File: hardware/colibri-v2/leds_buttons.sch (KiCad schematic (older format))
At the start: 39 parts

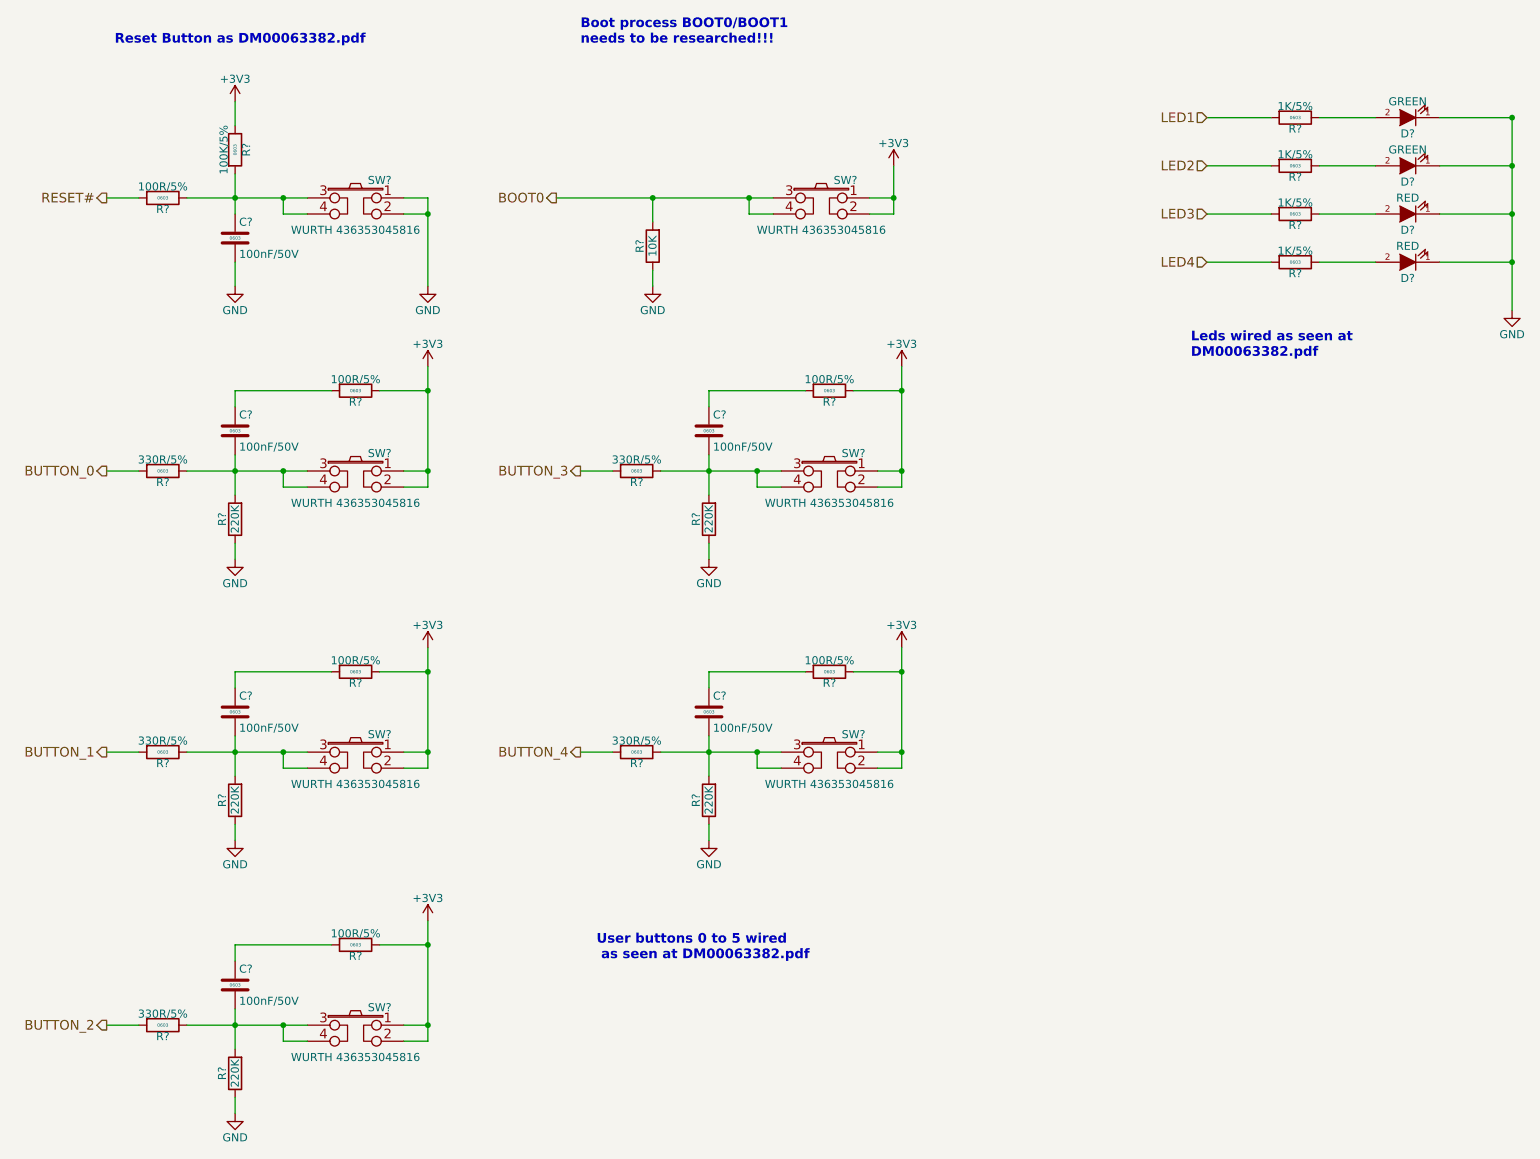
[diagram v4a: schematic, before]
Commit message: Worn on USB OTG connection for the cortex MCU
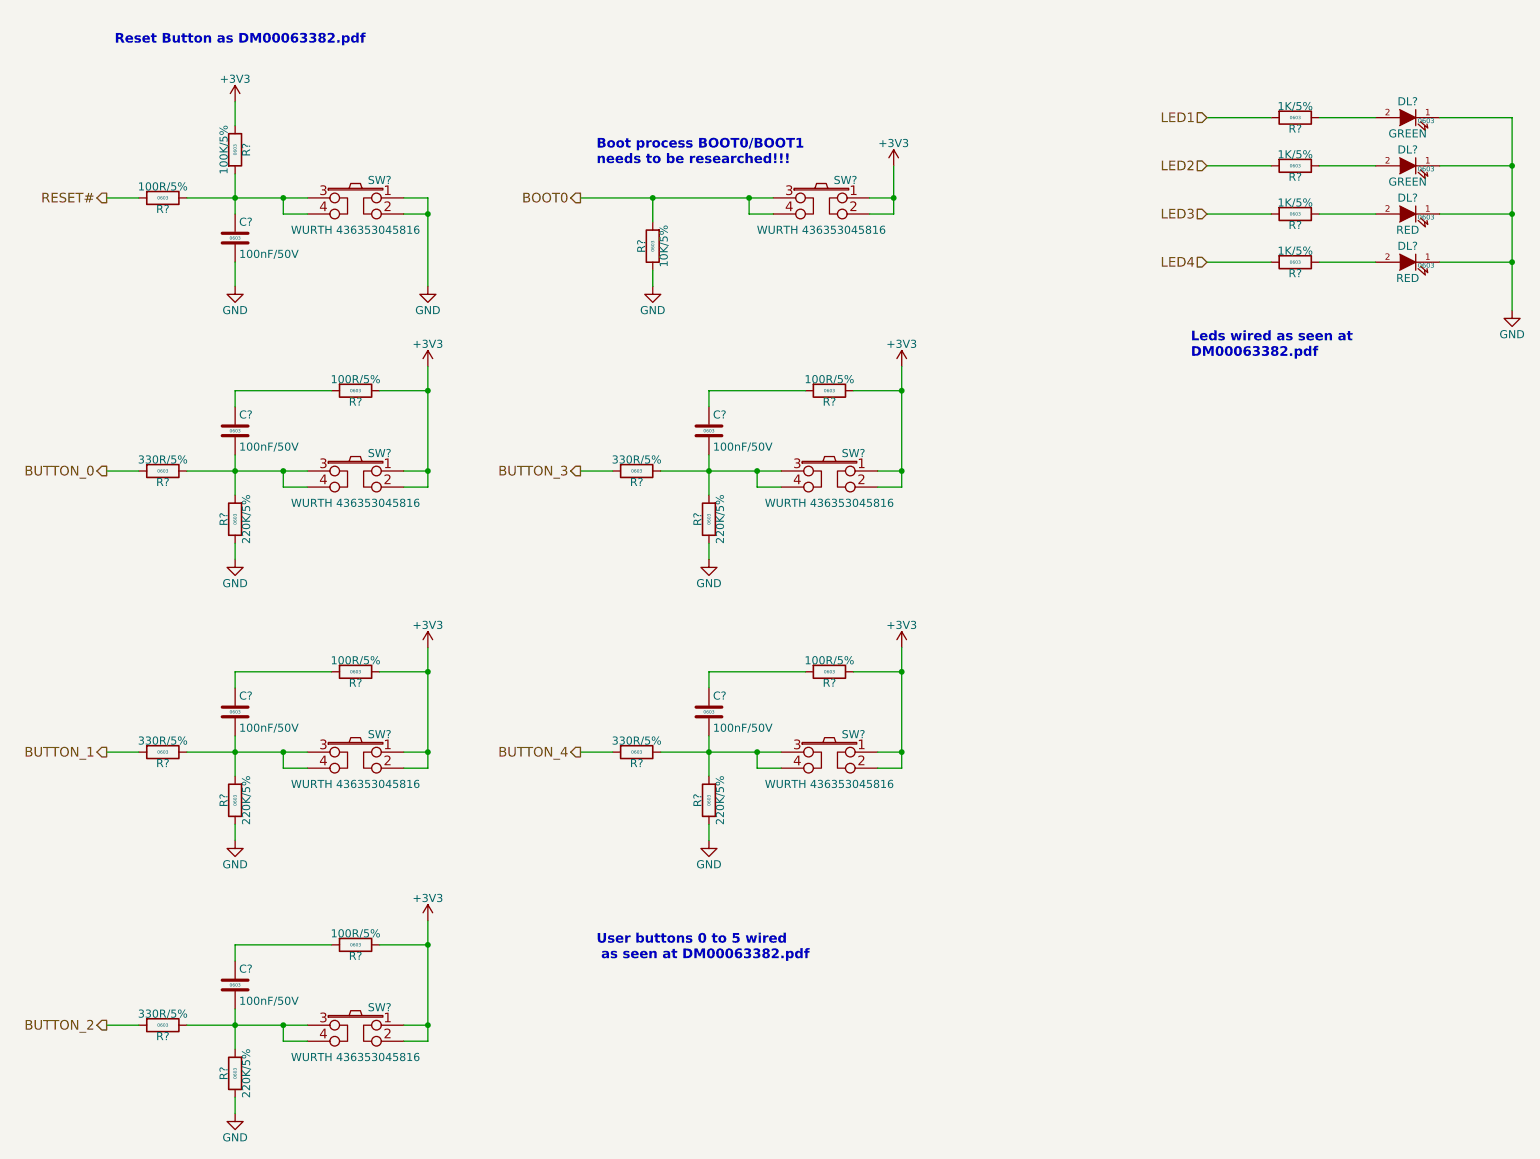
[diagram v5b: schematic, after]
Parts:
- removed D? (x2): GREEN, symbol LED
- removed D? (x2): RED, symbol LED
- removed R?: 10K, Resistors_SMD:R_0603, symbol R
- removed R? (x5): 220K, Resistors_SMD:R_0603, symbol R
- added DL? (x2): GREEN, LEDs:LED-0603, symbol LED_SMT
- added DL? (x2): RED, LEDs:LED-0603, symbol LED_SMT
- added R? (x5): 220K/5%, Resistors_SMD:R_0603, symbol R_SMT
- added R?: 10K/5%, Resistors_SMD:R_0603, symbol R_SMT
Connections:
- net BOOT0: now also R?.2
- net GND: now also DL?.1 (K), DL?.1 (K), DL?.1 (K), DL?.1 (K), R?.1, R?.1, R?.1, R?.1, R?.1, R?.1
- net at R?.1: now also DL?.2 (A) (x4)
- net at C?.2, R?.1, SW?.3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: now also R?.2 (x5)
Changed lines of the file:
@@
 Text HLabel 1350 1700 0    60   Output ~ 0
 RESET#
-$Comp
-L LED D?
-U 1 1 55862ED2
-P 9450 1200
-F 0 "D?" H 9450 1300 50  0000 C CNN
-F 1 "GREEN" H 9450 1100 50  0000 C CNN
-F 2 "" H 9450 1200 60  0001 C CNN
-F 3 "" H 9450 1200 60  0000 C CNN
-	1    9450 1200
-	-1   0    0    1
-$EndComp
-$Comp
-L LED D?
-U 1 1 55863115
-P 9450 1500
-F 0 "D?" H 9450 1600 50  0000 C CNN
-F 1 "GREEN" H 9450 1400 50  0000 C CNN
-F 2 "" H 9450 1500 60  0001 C CNN
-F 3 "" H 9450 1500 60  0000 C CNN
-	1    9450 1500
-	-1   0    0    1
-$EndComp
-$Comp
-L LED D?
-U 1 1 55863212
-P 9450 1800
-F 0 "D?" H 9450 1900 50  0000 C CNN
-F 1 "RED" H 9450 1700 50  0000 C CNN
-F 2 "" H 9450 1800 60  0001 C CNN
-F 3 "" H 9450 1800 60  0000 C CNN
-	1    9450 1800
-	-1   0    0    1
-$EndComp
-$Comp
-L LED D?
-U 1 1 558632D0
-P 9450 2100
-F 0 "D?" H 9450 2200 50  0000 C CNN
-F 1 "RED" H 9450 2000 50  0000 C CNN
-F 2 "" H 9450 2100 60  0001 C CNN
-F 3 "" H 9450 2100 60  0000 C CNN
-	1    9450 2100
-	-1   0    0    1
-$EndComp
 Text HLabel 8200 1200 0    60   Input ~ 0
 LED1
@@
 	1    0    0    -1
 $EndComp
-Text HLabel 4150 1700 0    60   Output ~ 0
+Text HLabel 4300 1700 0    60   Output ~ 0
 BOOT0
-$Comp
-L R R?
-U 1 1 5622C644
-P 4750 2000
-F 0 "R?" V 4830 2000 50  0000 C CNN
-F 1 "10K" V 4750 2000 50  0000 C CNN
-F 2 "Resistors_SMD:R_0603" V 4680 2000 30  0001 C CNN
-F 3 "" H 4750 2000 30  0000 C CNN
-	1    4750 2000
-	-1   0    0    1
-$EndComp
 $Comp
 L GND #PWR?
@@
 $EndComp
 Wire Wire Line
-	3350 2250 3350 1700
+	3350 1700 3350 2250
 Wire Wire Line
 	3350 1700 3200 1700
-Wire Wire Line
-	10100 1200 9650 1200
 Wire Wire Line
 	9650 1500 10100 1500
@@
 Wire Wire Line
 	1850 1700 2600 1700
-Connection ~ 10100 1200
 Wire Wire Line
 	6100 1700 6250 1700
@@
 	6250 1500 6250 1800
 Wire Wire Line
-	4150 1700 5500 1700
+	4300 1700 5500 1700
 Wire Wire Line
 	4750 1850 4750 1700
@@
 	1    0    0    -1
 $EndComp
-Text Notes 4300 750  0    60   ~ 12
-Boot process BOOT0/BOOT1\nneeds to be researched!!!
 $Comp
 L R_SMT R?
@@
 	1    0    0    -1
 $EndComp
-$Comp
-L R R?
-U 1 1 5628979B
-P 2150 5450
-F 0 "R?" V 2230 5450 50  0000 C CNN
-F 1 "220K" V 2150 5450 50  0000 C CNN
-F 2 "Resistors_SMD:R_0603" V 2080 5450 30  0001 C CNN
-F 3 "" H 2150 5450 30  0000 C CNN
-	1    2150 5450
-	-1   0    0    1
-$EndComp
 Wire Wire Line
 	2150 5700 2150 5600
@@
 	1    0    0    -1
 $EndComp
-$Comp
-L R R?
-U 1 1 5628DEFD
-P 2150 3700
-F 0 "R?" V 2230 3700 50  0000 C CNN
-F 1 "220K" V 2150 3700 50  0000 C CNN
-F 2 "Resistors_SMD:R_0603" V 2080 3700 30  0001 C CNN
-F 3 "" H 2150 3700 30  0000 C CNN
-	1    2150 3700
-	-1   0    0    1
-$EndComp
 Wire Wire Line
 	2150 3950 2150 3850
@@
 	1    0    0    -1
 $EndComp
-$Comp
-L R R?
-U 1 1 5628E114
-P 2150 7150
-F 0 "R?" V 2230 7150 50  0000 C CNN
-F 1 "220K" V 2150 7150 50  0000 C CNN
-F 2 "Resistors_SMD:R_0603" V 2080 7150 30  0001 C CNN
-F 3 "" H 2150 7150 30  0000 C CNN
-	1    2150 7150
-	-1   0    0    1
-$EndComp
 Wire Wire Line
 	2150 7400 2150 7300
@@
 	1    0    0    -1
 $EndComp
-$Comp
-L R R?
-U 1 1 5628E321
-P 5100 3700
-F 0 "R?" V 5180 3700 50  0000 C CNN
-F 1 "220K" V 5100 3700 50  0000 C CNN
-F 2 "Resistors_SMD:R_0603" V 5030 3700 30  0001 C CNN
-F 3 "" H 5100 3700 30  0000 C CNN
-	1    5100 3700
-	-1   0    0    1
-$EndComp
 Wire Wire Line
 	5100 3950 5100 3850
@@
 	1    0    0    -1
 $EndComp
-$Comp
-L R R?
-U 1 1 5628E52E
-P 5100 5450
-F 0 "R?" V 5180 5450 50  0000 C CNN
-F 1 "220K" V 5100 5450 50  0000 C CNN
-F 2 "Resistors_SMD:R_0603" V 5030 5450 30  0001 C CNN
-F 3 "" H 5100 5450 30  0000 C CNN
-	1    5100 5450
-	-1   0    0    1
-$EndComp
 Wire Wire Line
 	5100 5700 5100 5600
@@
 	2450 1800 2450 1700
 Connection ~ 2450 1700
+$Comp
+L R_SMT R?
+U 1 1 5631C3FC
+P 2150 3700
+F 0 "R?" V 2220 3700 50  0000 C CNN
+F 1 "220K/5%" V 2080 3700 50  0000 C CNN
+F 2 "Resistors_SMD:R_0603" V 2300 3700 30  0001 C CNN
+F 3 "" V 2230 3700 30  0000 C CNN
+F 4 "0603" V 2150 3700 20  0000 C CNN "SMT"
+F 5 "9331930" V 2350 3700 30  0001 C CNN "Part"
+F 6 "Farnell" V 2400 3700 30  0001 C CNN "Provider"
+	1    2150 3700
+	-1   0    0    1
+$EndComp
+$Comp
+L R_SMT R?
+U 1 1 5631C8F8
+P 2150 5450
+F 0 "R?" V 2220 5450 50  0000 C CNN
+F 1 "220K/5%" V 2080 5450 50  0000 C CNN
+F 2 "Resistors_SMD:R_0603" V 2300 5450 30  0001 C CNN
+F 3 "" V 2230 5450 30  0000 C CNN
+F 4 "0603" V 2150 5450 20  0000 C CNN "SMT"
+F 5 "9331930" V 2350 5450 30  0001 C CNN "Part"
+F 6 "Farnell" V 2400 5450 30  0001 C CNN "Provider"
+	1    2150 5450
+	-1   0    0    1
+$EndComp
+$Comp
+L R_SMT R?
+U 1 1 5631CA2A
+P 2150 7150
+F 0 "R?" V 2220 7150 50  0000 C CNN
+F 1 "220K/5%" V 2080 7150 50  0000 C CNN
+F 2 "Resistors_SMD:R_0603" V 2300 7150 30  0001 C CNN
+F 3 "" V 2230 7150 30  0000 C CNN
+F 4 "0603" V 2150 7150 20  0000 C CNN "SMT"
+F 5 "9331930" V 2350 7150 30  0001 C CNN "Part"
+F 6 "Farnell" V 2400 7150 30  0001 C CNN "Provider"
+	1    2150 7150
+	-1   0    0    1
+$EndComp
+$Comp
+L R_SMT R?
+U 1 1 5631CDD1
+P 5100 5450
+F 0 "R?" V 5170 5450 50  0000 C CNN
+F 1 "220K/5%" V 5030 5450 50  0000 C CNN
+F 2 "Resistors_SMD:R_0603" V 5250 5450 30  0001 C CNN
+F 3 "" V 5180 5450 30  0000 C CNN
+F 4 "0603" V 5100 5450 20  0000 C CNN "SMT"
+F 5 "9331930" V 5300 5450 30  0001 C CNN "Part"
+F 6 "Farnell" V 5350 5450 30  0001 C CNN "Provider"
+	1    5100 5450
+	-1   0    0    1
+$EndComp
+$Comp
+L R_SMT R?
+U 1 1 5631CF49
+P 5100 3700
+F 0 "R?" V 5170 3700 50  0000 C CNN
+F 1 "220K/5%" V 5030 3700 50  0000 C CNN
+F 2 "Resistors_SMD:R_0603" V 5250 3700 30  0001 C CNN
+F 3 "" V 5180 3700 30  0000 C CNN
+F 4 "0603" V 5100 3700 20  0000 C CNN "SMT"
+F 5 "9331930" V 5300 3700 30  0001 C CNN "Part"
+F 6 "Farnell" V 5350 3700 30  0001 C CNN "Provider"
+	1    5100 3700
+	-1   0    0    1
+$EndComp
+Text Notes 4400 1500 0    60   ~ 12
+Boot process BOOT0/BOOT1\nneeds to be researched!!!
+$Comp
+L R_SMT R?
+U 1 1 5631DE54
+P 4750 2000
+F 0 "R?" V 4820 2000 50  0000 C CNN
+F 1 "10K/5%" V 4680 2000 50  0000 C CNN
+F 2 "Resistors_SMD:R_0603" V 4900 2000 30  0001 C CNN
+F 3 "" V 4830 2000 30  0000 C CNN
+F 4 "0603" V 4750 2000 20  0000 C CNN "SMT"
+F 5 "9331700" V 4950 2000 30  0001 C CNN "Part"
+F 6 "Farnell" V 5000 2000 30  0001 C CNN "Provider"
+	1    4750 2000
+	-1   0    0    1
+$EndComp
+$Comp
+L LED_SMT DL?
+U 1 1 5631FE41
+P 9450 1200
+F 0 "DL?" H 9450 1300 50  0000 C CNN
+F 1 "GREEN" H 9450 1100 50  0000 C CNN
+F 2 "LEDs:LED-0603" H 9450 1050 30  0001 C CNN
+F 3 "" H 9450 1200 60  0000 C CNN
+F 4 "0603" H 9335 1180 30  0000 C CNN "SMT"
+F 5 "2322070" H 9450 1000 30  0001 C CNN "Part"
+F 6 "Farnell" H 9450 950 30  0001 C CNN "Provider"
+	1    9450 1200
+	-1   0    0    -1
+$EndComp
+$Comp
+L LED_SMT DL?
+U 1 1 563203FE
+P 9450 1500
+F 0 "DL?" H 9450 1600 50  0000 C CNN
+F 1 "GREEN" H 9450 1400 50  0000 C CNN
+F 2 "LEDs:LED-0603" H 9450 1350 30  0001 C CNN
+F 3 "" H 9450 1500 60  0000 C CNN
+F 4 "0603" H 9335 1480 30  0000 C CNN "SMT"
+F 5 "2322070" H 9450 1300 30  0001 C CNN "Part"
+F 6 "Farnell" H 9450 1250 30  0001 C CNN "Provider"
+	1    9450 1500
+	-1   0    0    -1
+$EndComp
+$Comp
+L LED_SMT DL?
+U 1 1 5632048F
+P 9450 1800
+F 0 "DL?" H 9450 1900 50  0000 C CNN
+F 1 "RED" H 9450 1700 50  0000 C CNN
+F 2 "LEDs:LED-0603" H 9450 1650 30  0001 C CNN
+F 3 "" H 9450 1800 60  0000 C CNN
+F 4 "0603" H 9335 1780 30  0000 C CNN "SMT"
+F 5 "2322071" H 9450 1600 30  0001 C CNN "Part"
+F 6 "Farnell" H 9450 1550 30  0001 C CNN "Provider"
+	1    9450 1800
+	-1   0    0    -1
+$EndComp
+$Comp
+L LED_SMT DL?
+U 1 1 563205A7
+P 9450 2100
+F 0 "DL?" H 9450 2200 50  0000 C CNN
+F 1 "RED" H 9450 2000 50  0000 C CNN
+F 2 "LEDs:LED-0603" H 9450 1950 30  0001 C CNN
+F 3 "" H 9450 2100 60  0000 C CNN
+F 4 "0603" H 9335 2080 30  0000 C CNN "SMT"
+F 5 "2322071" H 9450 1900 30  0001 C CNN "Part"
+F 6 "Farnell" H 9450 1850 30  0001 C CNN "Provider"
+	1    9450 2100
+	-1   0    0    -1
+$EndComp
+Wire Wire Line
+	9650 1200 10100 1200
 $EndSCHEMATC

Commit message: Work on Cortex wiring
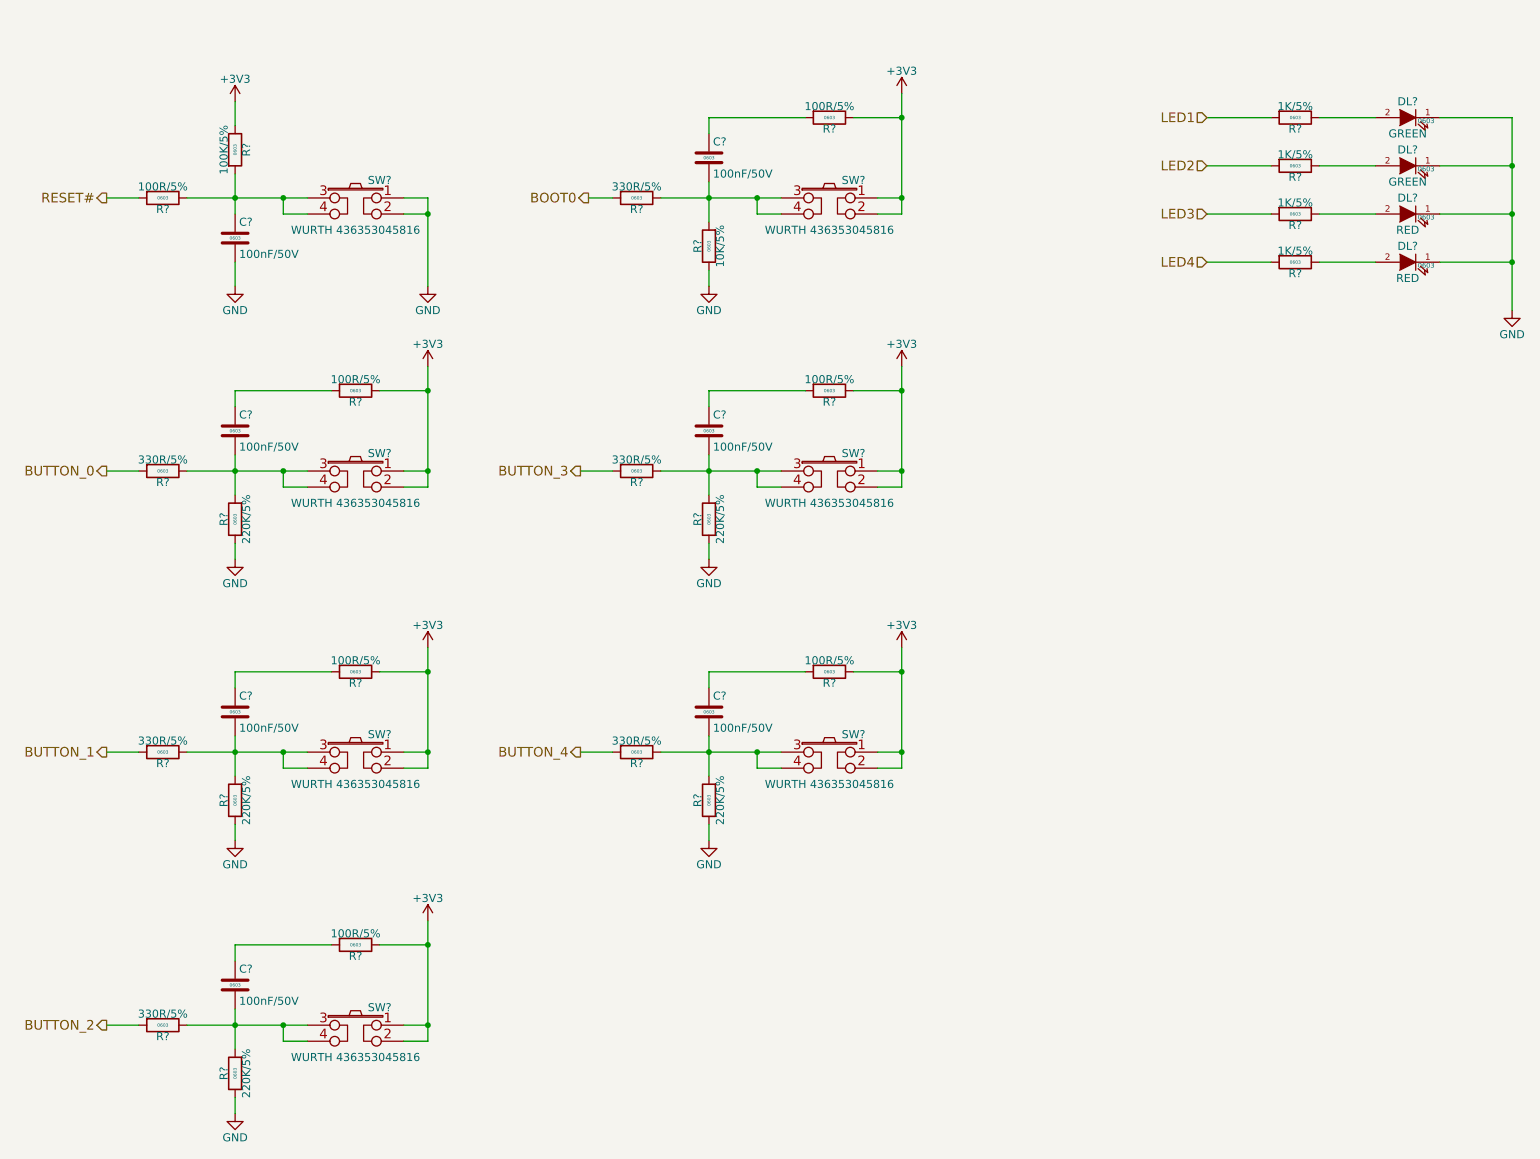
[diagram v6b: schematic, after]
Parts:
- added C?: 100nF/50V, Capacitors_SMD:C_0603, symbol C_SMT
- added R?: 100R/5%, Resistors_SMD:R_0603, symbol R_SMT
- added R?: 330R/5%, Resistors_SMD:R_0603, symbol R_SMT
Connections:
- net +3V3: now also R?.1
- net BOOT0: now also R?.2; no longer R?.2, SW?.3, SW?.4
- new net: C?.2, R?.1, R?.2, SW?.3, SW?.4
- new net: C?.1, R?.2
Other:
- note removed: "Boot process BOOT0/BOOT1\nneeds to be researched!!!"
- note removed: "Leds wired as seen at\nDM00063382.pdf"
- note removed: "Reset Button as DM00063382.pdf"
- note removed: "User buttons 0 to 5 wired\n as seen at DM00063382.pdf"
- moved on the sheet: R?, SW?
